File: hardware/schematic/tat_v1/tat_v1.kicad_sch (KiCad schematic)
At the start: 0 parts

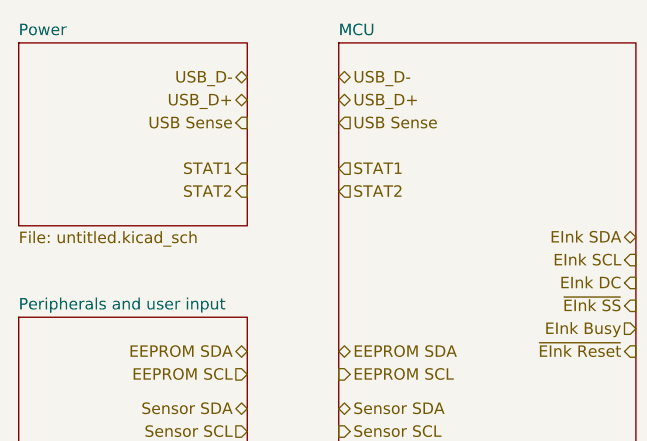
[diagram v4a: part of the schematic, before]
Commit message: Added measuring battery voltage using the ADC. Basic schematic is complete, needs checking and refinement
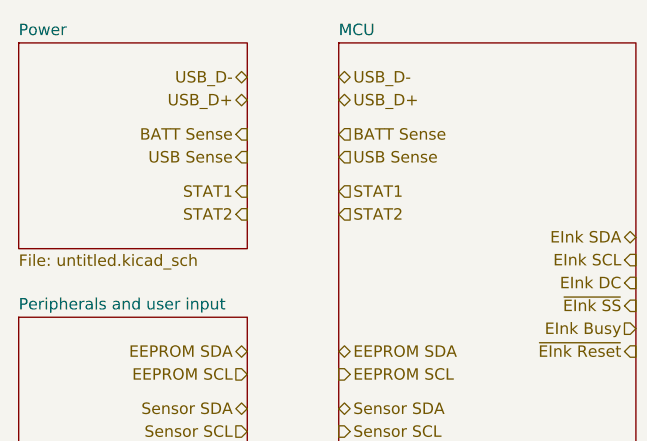
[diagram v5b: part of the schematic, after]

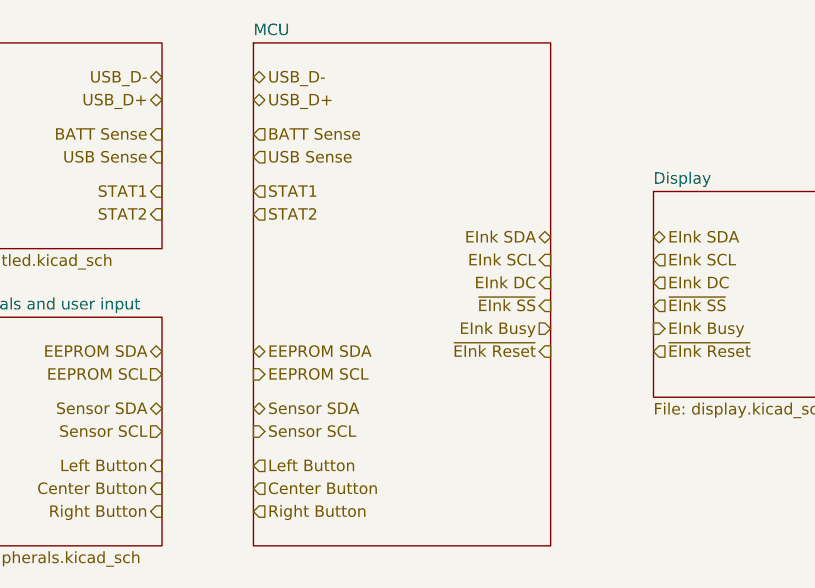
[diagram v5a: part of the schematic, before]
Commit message: Cleaned up basic schematic and double checked all components. Need to complete ERC.
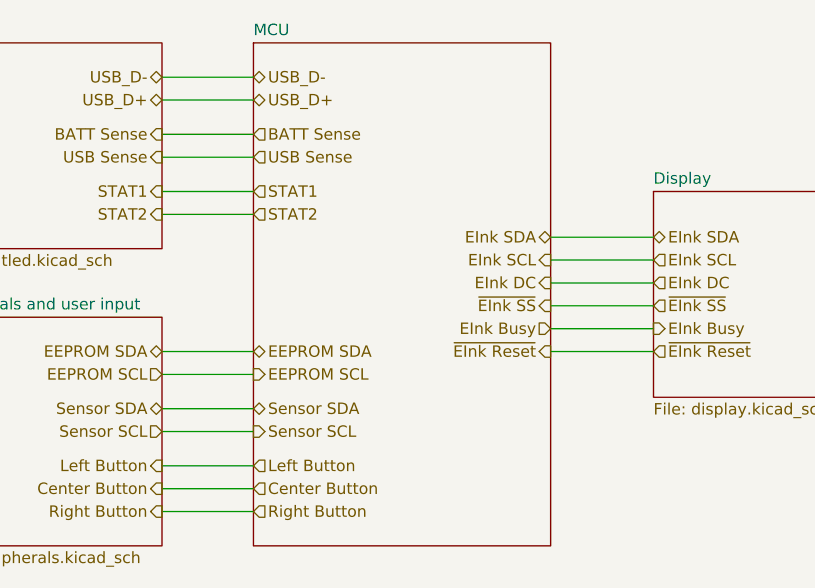
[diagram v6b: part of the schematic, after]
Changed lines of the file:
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@@
 		(rev "v1.0")
+	)
+	(wire
+		(pts
+			(xy 113.03 137.16) (xy 123.19 137.16)
+		)
+		(stroke
+			(width 0)
+			(type default)
+		)
+	)
+	(wire
+		(pts
+			(xy 156.21 123.19) (xy 167.64 123.19)
+		)
+		(stroke
+			(width 0)
+			(type default)
+		)
+	)
+	(wire
+		(pts
+			(xy 156.21 130.81) (xy 167.64 130.81)
+		)
+		(stroke
+			(width 0)
+			(type default)
+		)
+	)
+	(wire
+		(pts
+			(xy 113.03 113.03) (xy 123.19 113.03)
+		)
+		(stroke
+			(width 0)
+			(type default)
+		)
+	)
+	(wire
+		(pts
+			(xy 113.03 143.51) (xy 123.19 143.51)
+		)
+		(stroke
+			(width 0)
+			(type default)
+		)
+	)
+	(wire
+		(pts
+			(xy 156.21 128.27) (xy 167.64 128.27)
+		)
+		(stroke
+			(width 0)
+			(type default)
+		)
+	)
+	(wire
+		(pts
+			(xy 113.03 102.87) (xy 123.19 102.87)
+		)
+		(stroke
+			(width 0)
+			(type default)
+		)
+	)
+	(wire
+		(pts
+			(xy 113.03 130.81) (xy 123.19 130.81)
+		)
+		(stroke
+			(width 0)
+			(type default)
+		)
+	)
+	(wire
+		(pts
+			(xy 113.03 146.05) (xy 123.19 146.05)
+		)
+		(stroke
+			(width 0)
+			(type default)
+		)
+	)
+	(wire
+		(pts
+			(xy 113.03 148.59) (xy 123.19 148.59)
+		)
+		(stroke
+			(width 0)
+			(type default)
+		)
+	)
+	(wire
+		(pts
+			(xy 156.21 125.73) (xy 167.64 125.73)
+		)
+		(stroke
+			(width 0)
+			(type default)
+		)
+	)
+	(wire
+		(pts
+			(xy 113.03 106.68) (xy 123.19 106.68)
+		)
+		(stroke
+			(width 0)
+			(type default)
+		)
+	)
+	(wire
+		(pts
+			(xy 156.21 120.65) (xy 167.64 120.65)
+		)
+		(stroke
+			(width 0)
+			(type default)
+		)
+	)
+	(wire
+		(pts
+			(xy 113.03 109.22) (xy 123.19 109.22)
+		)
+		(stroke
+			(width 0)
+			(type default)
+		)
+	)
+	(wire
+		(pts
+			(xy 156.21 118.11) (xy 167.64 118.11)
+		)
+		(stroke
+			(width 0)
+			(type default)
+		)
+	)
+	(wire
+		(pts
+			(xy 113.03 139.7) (xy 123.19 139.7)
+		)
+		(stroke
+			(width 0)
+			(type default)
+		)
+	)
+	(wire
+		(pts
+			(xy 113.03 115.57) (xy 123.19 115.57)
+		)
+		(stroke
+			(width 0)
+			(type default)
+		)
+	)
+	(wire
+		(pts
+			(xy 113.03 100.33) (xy 123.19 100.33)
+		)
+		(stroke
+			(width 0)
+			(type default)
+		)
+	)
+	(wire
+		(pts
+			(xy 113.03 133.35) (xy 123.19 133.35)
+		)
+		(stroke
+			(width 0)
+			(type default)
+		)
 	)
 	(hierarchical_label "~{EInk Reset}"

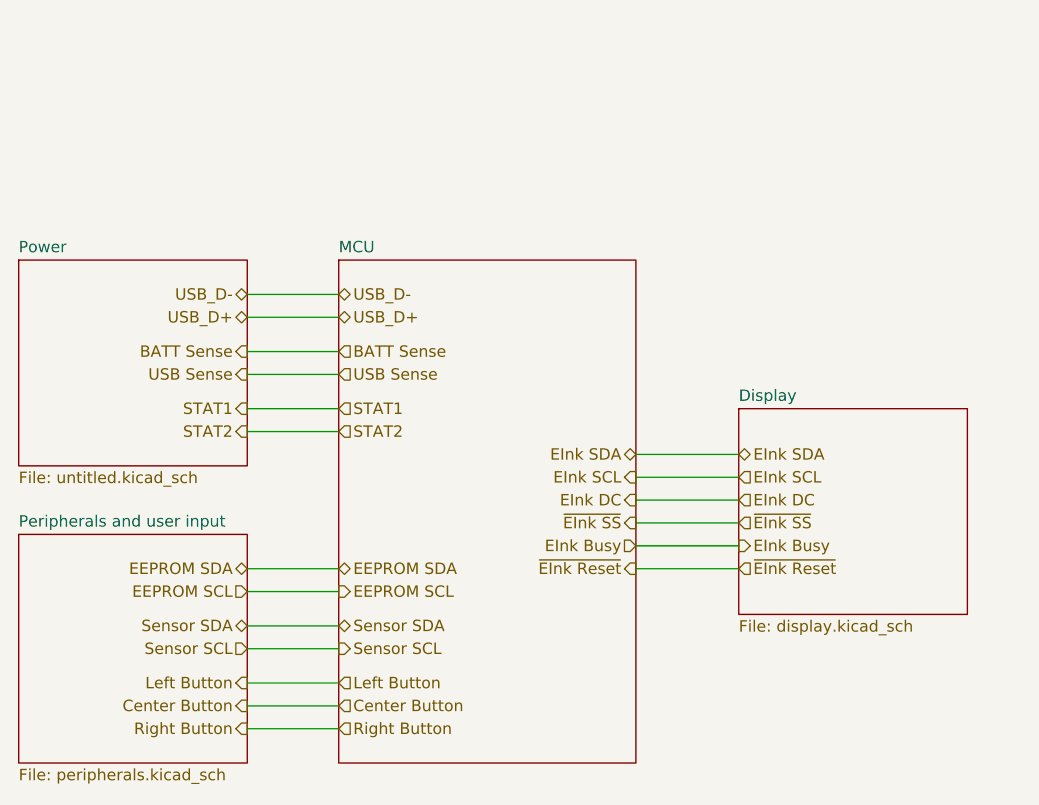
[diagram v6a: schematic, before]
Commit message: Added new titles to sheets
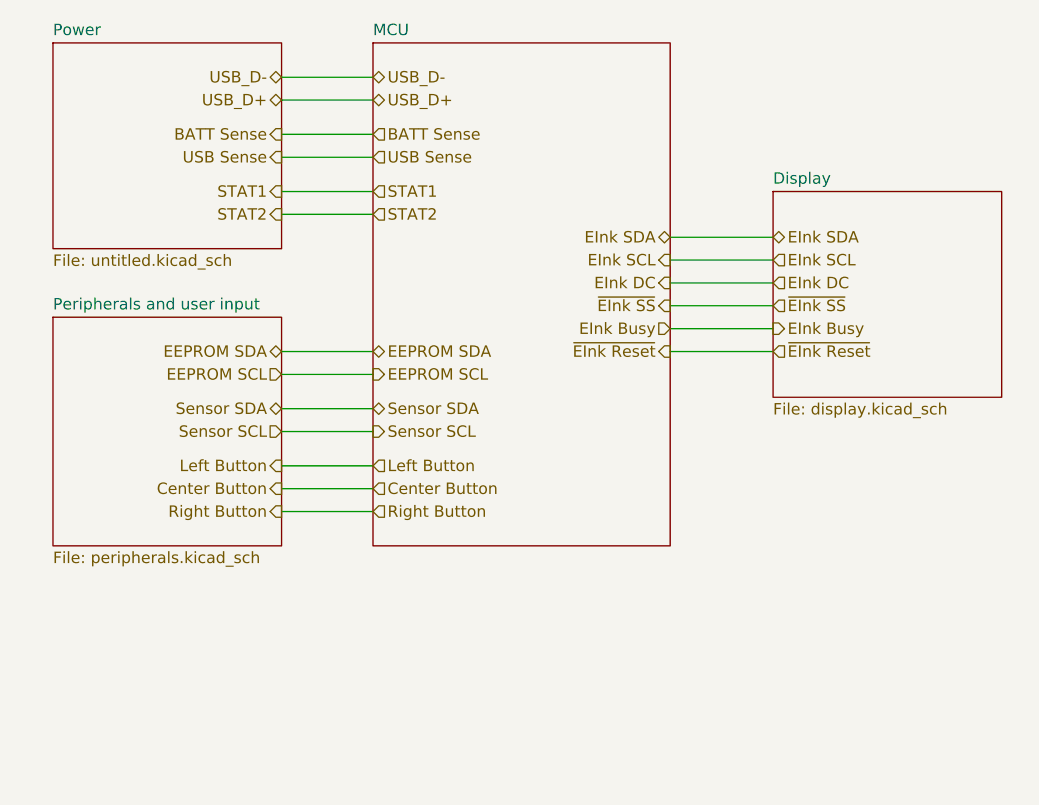
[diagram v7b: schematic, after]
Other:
- title: Tiny Ambient Tracker -> Tiny Ambient Tracker - root schematic

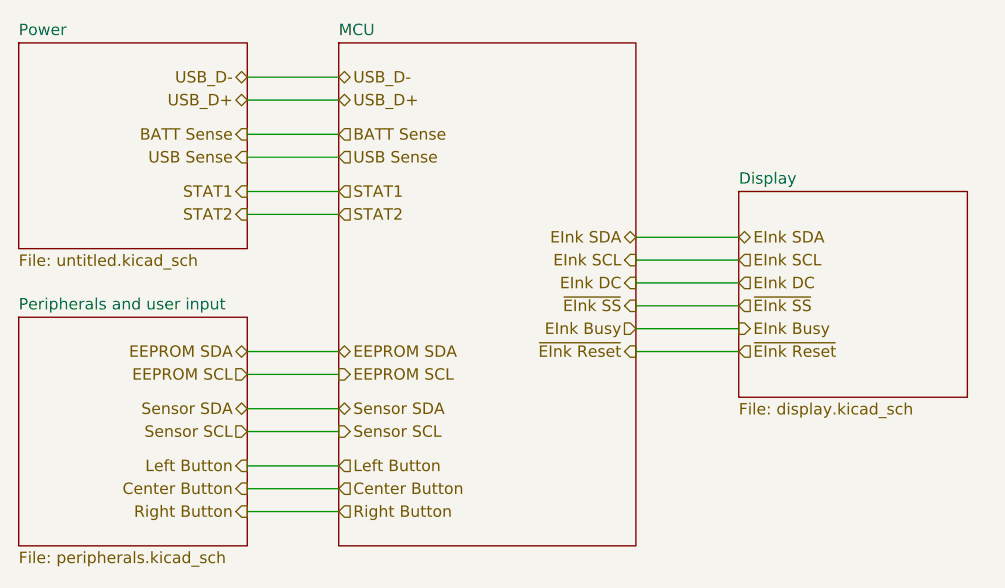
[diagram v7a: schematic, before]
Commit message: Synced hierarchical pins to sheets, need to fix rest of ERC errors
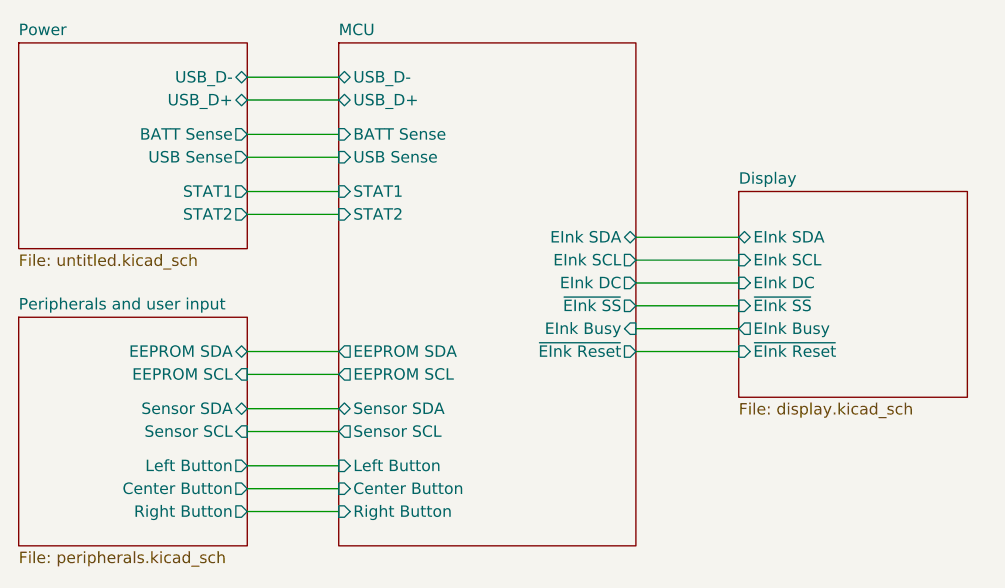
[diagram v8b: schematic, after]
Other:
- sheet Display ports: added EInk Busy, EInk DC, EInk SCL, EInk SDA, ~{EInk Reset}, ~{EInk SS}; removed none
- sheet MCU ports: added BATT Sense, Center Button, EEPROM SCL, EEPROM SDA, EInk Busy, EInk DC, EInk SCL, EInk SDA, Left Button, Right Button, STAT1, STAT2, Sensor SCL, Sensor SDA, USB Sense, USB_D+, USB_D-, ~{EInk Reset}, ~{EInk SS}; removed none
- sheet Peripherals and user input ports: added Center Button, EEPROM SCL, EEPROM SDA, Left Button, Right Button, Sensor SCL, Sensor SDA; removed none
- sheet Power ports: added BATT Sense, STAT1, STAT2, USB Sense, USB_D+, USB_D-; removed none
